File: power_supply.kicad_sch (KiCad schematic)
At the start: 0 parts

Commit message: Power supply initial schematic
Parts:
- added BT?: 4xAA, symbol Device:Battery
- added C?: 100pF, symbol Device:C
- added C? (x2): 100nF, symbol Device:C
- added C?: 2.2nF, symbol Device:C
- added C? (x2): 33uF, symbol Device:C_Polarized
- added C?: 47uF, symbol Device:C_Polarized
- added D?: GREEN, symbol Device:LED
- added D?: SKL34, symbol Device:D_Schottky
- added F?: 2A, symbol Device:Polyfuse
- added L?: 3.3uH, symbol Device:L
- added Q?: SI4368, symbol Simulation_SPICE:NMOS
- added R?: 1MR, symbol Device:R
- added R?: 10.2kR, symbol Device:R
- added R?: 53.6kR, symbol Device:R
- added R?: 18kR, symbol Device:R
- added R?: 20mR, symbol Device:R
- added SW?: POWER, symbol Switch:SW_SPDT
- added U?: LTC3872, symbol Autko:LTC3872
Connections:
- new net: C?.1, R?.2, U?.7 (RUN/SS)
- new net: C?.1, C?.1, D?.1 (K), F?.1, R?.1
- new net: BT?.1 (+), SW?.2 (B)
- new net: C?.1, R?.2, U?.2 (ITH)
- new net: R?.1, R?.2, U?.3 (FB)
- new net: Q?.2 (G), U?.5 (NGATE)
- new net: Q?.3 (S), R?.1, U?.8 (SW)
- new net: D?.2 (A), L?.2, Q?.1 (D)
- new net: C?.1, R?.1
- new net +7.5V: F?.2
- new net +BATT: C?.1, C?.1, L?.1, R?.1, SW?.1 (A), U?.6 (VIN)
- new net GND: BT?.2 (-), C?.2, C?.2, C?.2, C?.2, C?.2, C?.2, C?.2, R?.2, R?.2, U?.1 (IPRG), U?.4 (GND)
- no-connect marks 0 -> 1

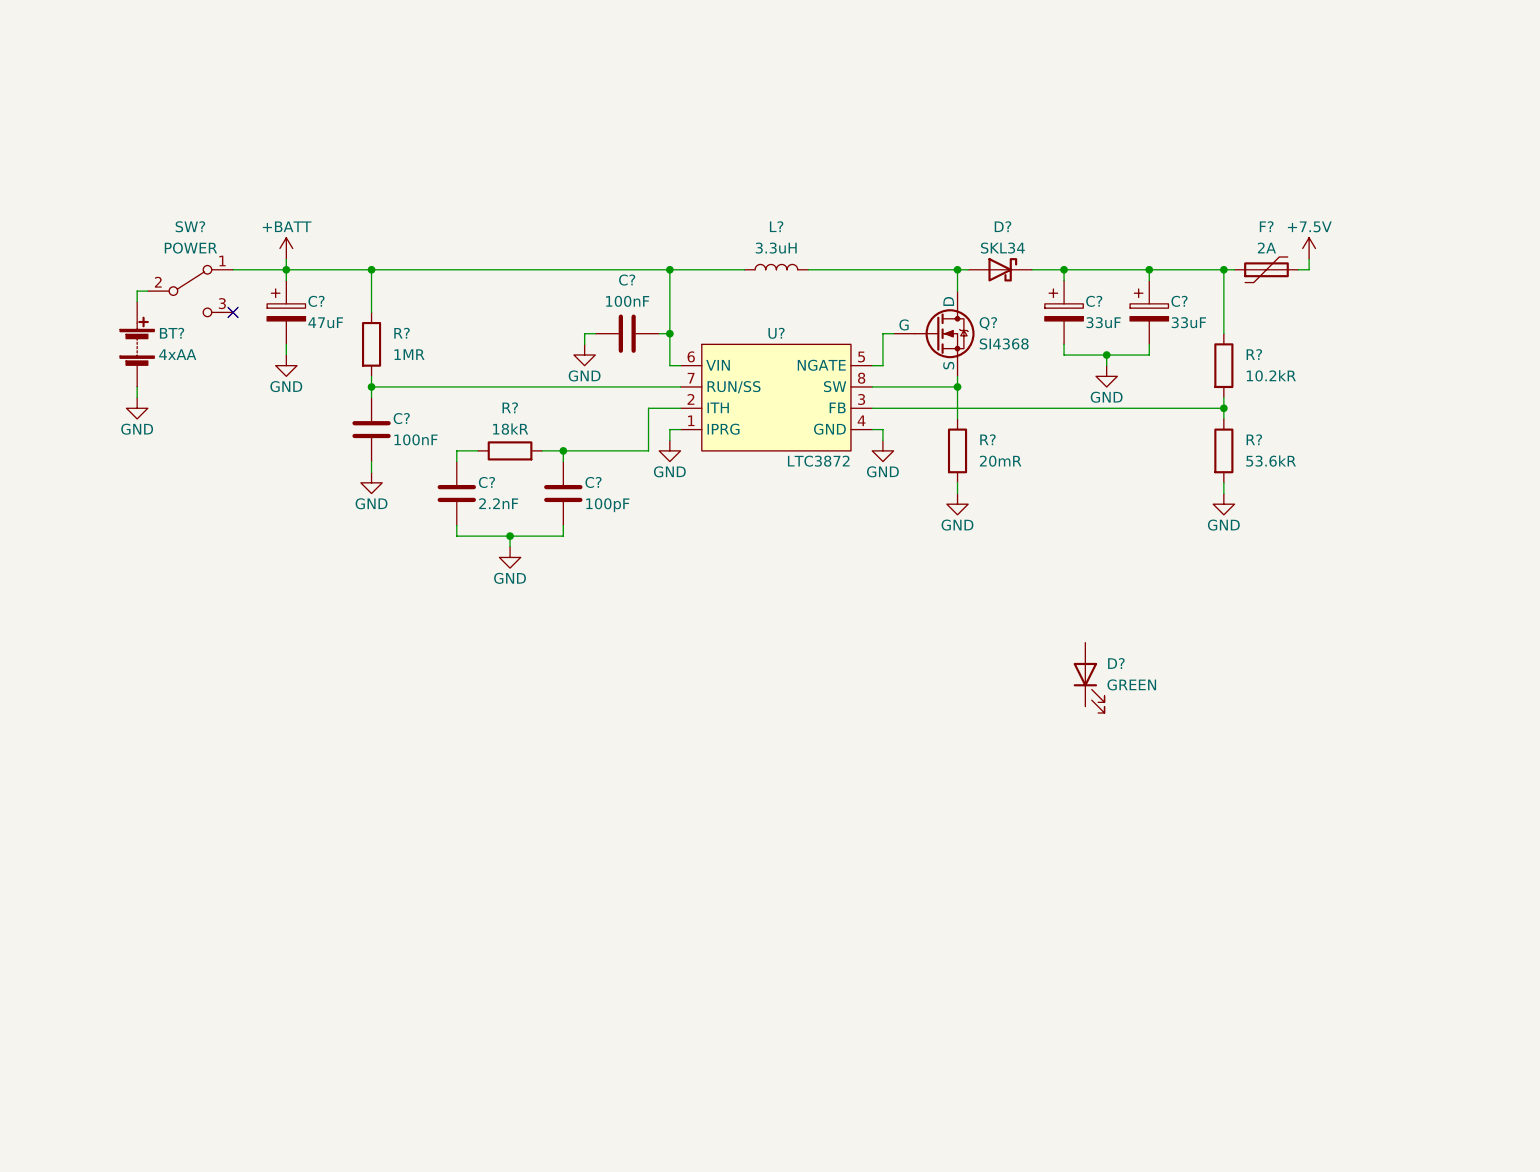
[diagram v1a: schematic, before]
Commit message: Power supply voltage regulators
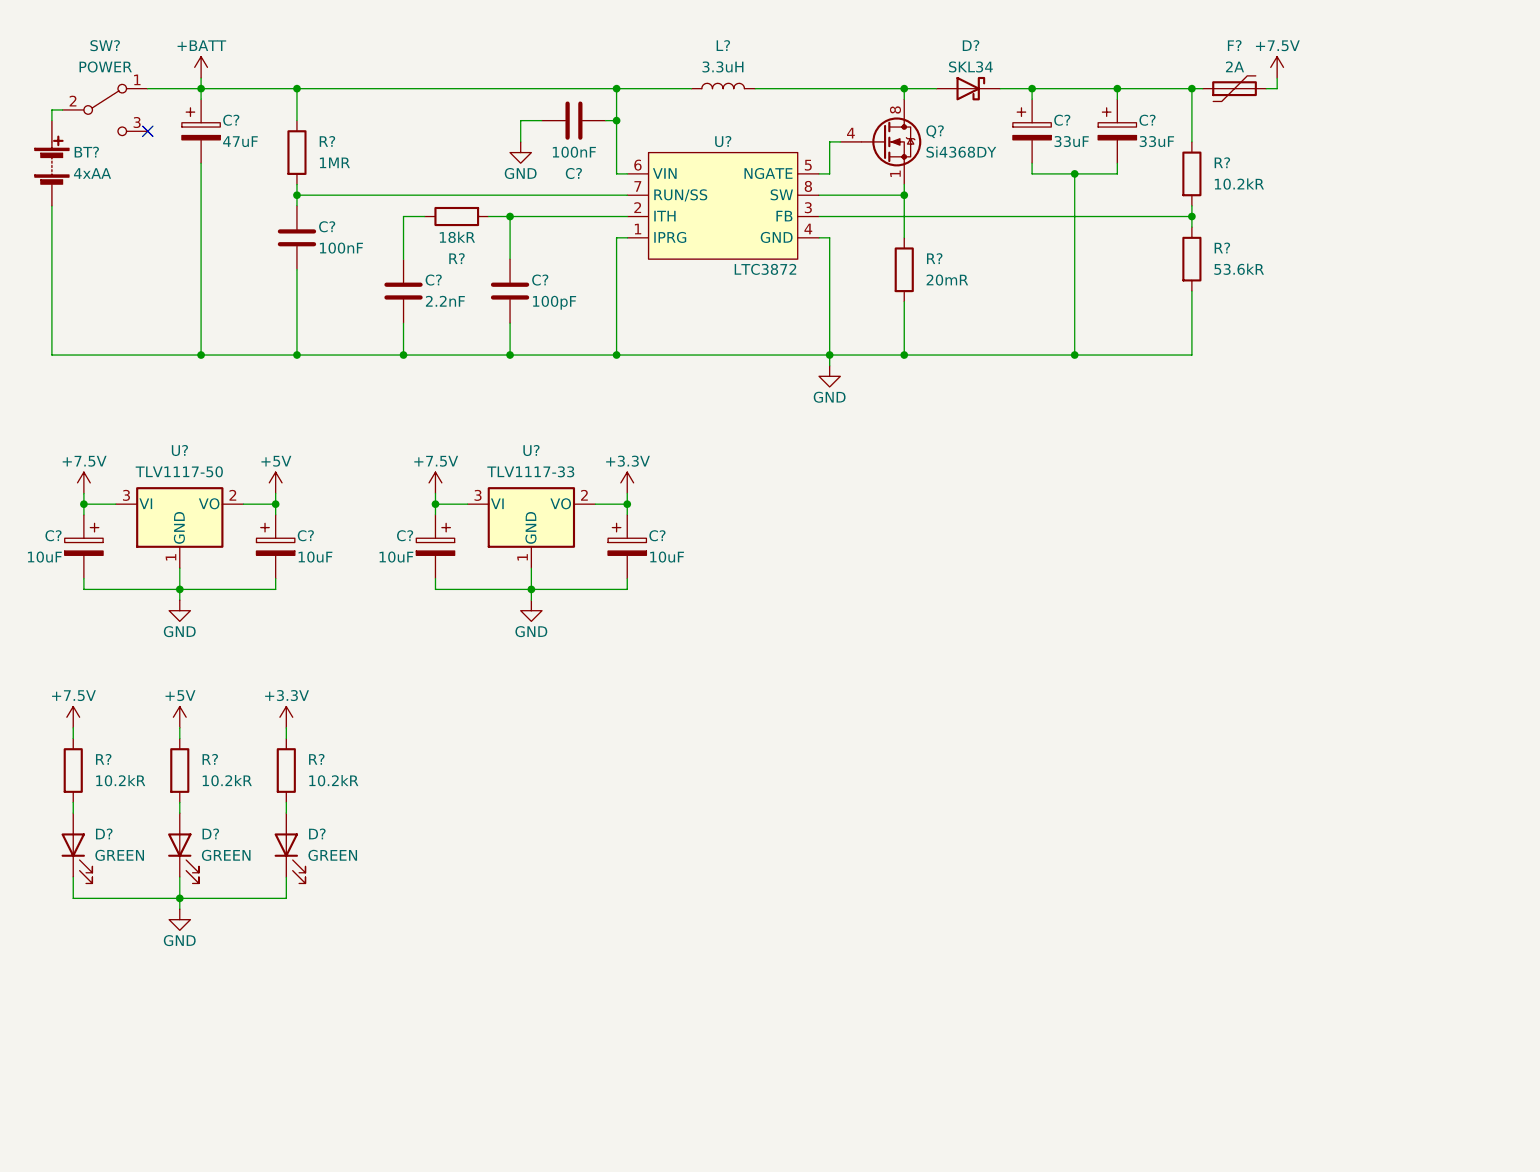
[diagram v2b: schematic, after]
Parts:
- removed BT?: 4xAA, symbol Device:Battery
- removed C?: 100pF, symbol Device:C
- removed C? (x2): 100nF, symbol Device:C
- removed C?: 2.2nF, symbol Device:C
- removed C? (x2): 33uF, symbol Device:C_Polarized
- removed C?: 47uF, symbol Device:C_Polarized
- removed D?: SKL34, symbol Device:D_Schottky
- removed F?: 2A, symbol Device:Polyfuse
- removed L?: 3.3uH, symbol Device:L
- removed Q?: SI4368, symbol Simulation_SPICE:NMOS
- removed R?: 1MR, symbol Device:R
- removed R?: 10.2kR, symbol Device:R
- removed R?: 53.6kR, symbol Device:R
- removed R?: 18kR, symbol Device:R
- removed R?: 20mR, symbol Device:R
- removed SW?: POWER, symbol Switch:SW_SPDT
- removed U?: LTC3872, symbol Autko:LTC3872
- added BT?: 4xAA, symbol Device:Battery
- added C? (x4): 10uF, symbol Device:C_Polarized
- added C? (x2): 100nF, symbol Device:C
- added C?: 100pF, symbol Device:C
- added C?: 2.2nF, symbol Device:C
- added C? (x2): 33uF, symbol Device:C_Polarized
- added C?: 47uF, symbol Device:C_Polarized
- added D? (x2): GREEN, symbol Device:LED
- added D?: SKL34, symbol Device:D_Schottky
- added F?: 2A, symbol Device:Polyfuse
- added L?: 3.3uH, symbol Device:L
- added Q?: Si4368DY, Package_SO:SO-8_3.9x4.9mm_P1.27mm, symbol Autko:Si4368DY
- added R?: 18kR, symbol Device:R
- added R? (x4): 10.2kR, symbol Device:R
- added R?: 53.6kR, symbol Device:R
- added R?: 1MR, symbol Device:R
- added R?: 20mR, symbol Device:R
- added SW?: POWER, symbol Switch:SW_SPDT
- added U?: LTC3872, symbol Autko:LTC3872
- added U?: TLV1117-50, symbol Regulator_Linear:TLV1117-50
- added U?: TLV1117-33, symbol Regulator_Linear:TLV1117-33
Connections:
- net +7.5V: now also C?.1, C?.1, F?.2, R?.1, U?.3 (VI), U?.3 (VI)
- net +BATT: now also C?.1, C?.1, L?.1, R?.1, SW?.1 (A), U?.6 (VIN)
- net GND: now also D?.1 (K), BT?.2 (-), C?.2, C?.2, C?.2, C?.2, C?.2, C?.2, C?.2, C?.2, C?.2, C?.2, C?.2, D?.1 (K), D?.1 (K), R?.2, R?.2, U?.1 (GND), U?.1 (GND), U?.1 (IPRG), U?.4 (GND)
- net at D?.2 (A): now also R?.2
- new net: C?.1, R?.2, U?.2 (ITH)
- new net: R?.1, R?.2, U?.3 (FB)
- new net: Q?.4 (G), U?.5 (NGATE)
- new net: C?.1, R?.2, U?.7 (RUN/SS)
- new net: Q?.1 (S), Q?.2 (S), Q?.3 (S), R?.1, U?.8 (SW)
- new net: BT?.1 (+), SW?.2 (B)
- new net: C?.1, R?.1
- new net: C?.1, C?.1, D?.1 (K), F?.1, R?.1
- new net: D?.2 (A), R?.2 (x2)
- new net: D?.2 (A), L?.2, Q?.5 (D), Q?.6 (D), Q?.7 (D), Q?.8 (D)
- new net +3.3V: C?.1, R?.1, U?.2 (VO)
- new net +5V: C?.1, R?.1, U?.2 (VO)
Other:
- moved on the sheet: D?

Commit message: Power supply schematic beautified
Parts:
- removed BT?: 4xAA, symbol Device:Battery
- removed C? (x2): 10uF, symbol Device:C_Polarized
- removed SW?: POWER, symbol Switch:SW_SPDT
- added BT?: 4xAA, symbol Device:Battery
- added C? (x2): 10uF, symbol Device:C_Polarized
- added SW?: POWER, symbol Switch:SW_SPDT
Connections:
- net +5V: now also C?.1
- net +7.5V: now also C?.1
- net +BATT: now also SW?.1 (A)
- net GND: now also BT?.2 (-), C?.2, C?.2
- new net: BT?.1 (+), SW?.2 (B)
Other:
- note added: "3.3V voltage regulator"
- note added: "5.0V voltage regulator"
- note added: "7.5V boost converter"
- note added: "Battery connector"
- note added: "Power indicators"
- moved on the sheet: C?, D?, F?, L?, Q?, R?, U?
